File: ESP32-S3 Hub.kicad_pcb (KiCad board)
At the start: 6 copper layers, 15 x 30 mm, 73 parts, among them J1 Precidip 853-87-004-20-001101, J10 Precidip 853-87-004-20-001101, J11 FPC 0.3mm Aces 51688-0070M, J12 Precidip 853-87-004-20-001101, J13 TE 3-2363961-0 receptacle, J15 Precidip 853-87-004-20-001101, J16 TE 3-2363961-0 receptacle, J18 Precidip 852-10-004-20-001101, J2 Precidip 853-87-004-20-001101, J3 FPC 0.3mm Aces 51688-0070M, J4 Precidip 853-87-004-20-001101, J5 FPC 0.3mm Aces 51688-0070M, J6 Precidip 853-87-004-20-001101, J7 Precidip 853-87-004-20-001101, J8 FPC 0.3mm Aces 51688-0070M, J9 Precidip 853-87-004-20-001101, SW1 Mitsumi R-667996, SW2 Mitsumi R-667996, U1 ESP32-S3 FN8, U2 SN74LV595A, U3 THVD1420DRLR, U4 TPS2521ARPWR, U5 SN74LV595A, U6 TS5A3159DCK, Y1 2 pin 40MHZ, 10ppm tol., 20pp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

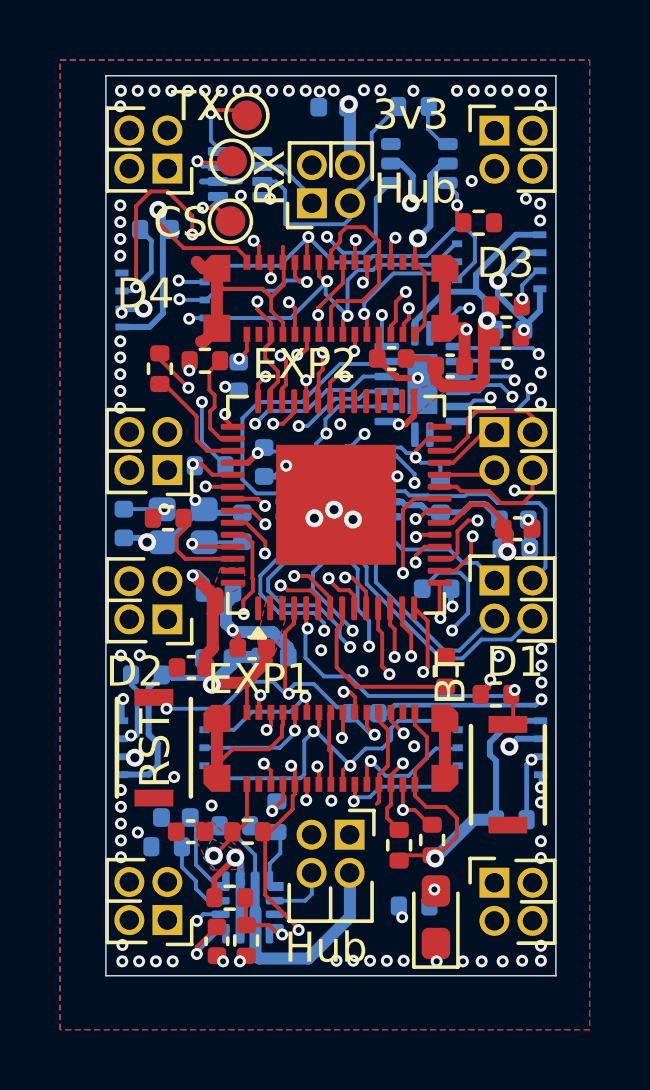
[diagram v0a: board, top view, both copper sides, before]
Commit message: Fixed clock to be on top only, moved to 0201, separate clock signals
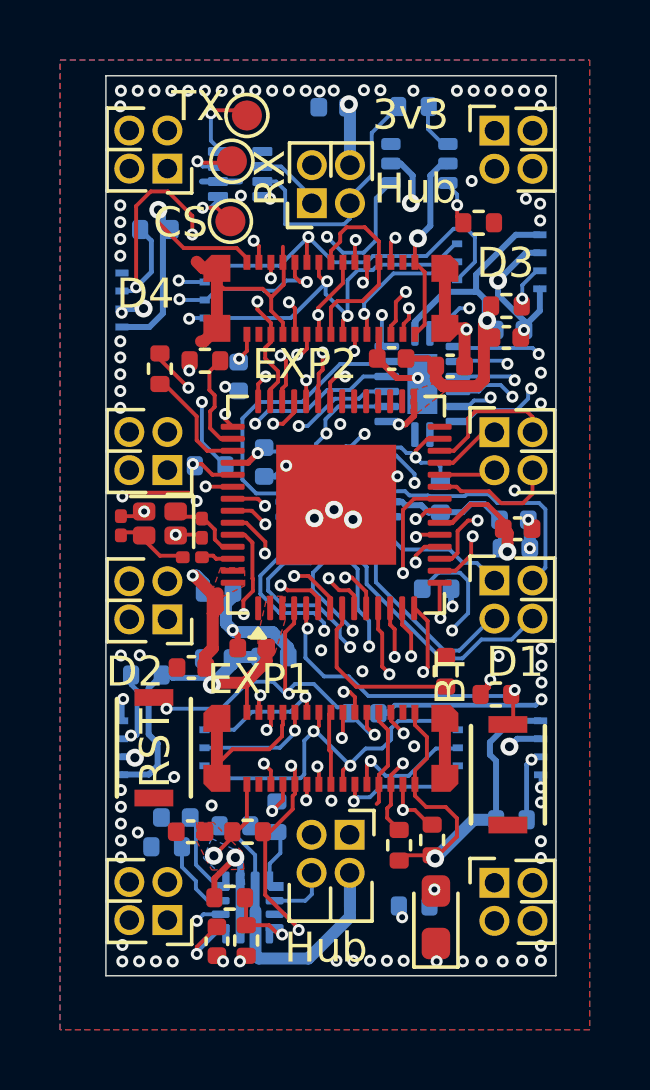
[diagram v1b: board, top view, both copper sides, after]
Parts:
- C11, C12: footprint Capacitor_SMD:C_0402_1005Metric -> Capacitor_SMD:C_0201_0603Metric; moved to F.Cu
- R6: footprint Resistor_SMD:R_0402_1005Metric -> Resistor_SMD:R_0201_0603Metric
- Y1: footprint Crystal:Crystal_SMD_2016-4Pin_2.0x1.6mm -> custom_Crystal:Crystal_SMD_1612-4Pin_1.6x1.2mm; moved to F.Cu
- moved R6 1.53 mm to (150.8, 97.8)
- moved C12 1.35 mm to (151.1, 96.9), turned to -90 degrees
- moved Y1 0.78 mm to (149.7, 96.7)
- moved C11 0.12 mm to (148.4, 96.8), turned to -90 degrees
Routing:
- net Net-(U1-XTAL_P): track 3.20 -> 0.95 mm
- net GND: track 85.2 -> 83.4 mm, vias 102 -> 104
- net Net-(C11-Pad2): track 1.76 -> 2.60 mm, vias 1 -> 0
- net Net-(U1-XTAL_N): track 2.67 -> 2.51 mm, vias 1 -> 0
